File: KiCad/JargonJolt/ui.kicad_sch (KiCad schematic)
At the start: 18 parts, among them J4 Conn_01x06, J5 Conn_01x06, J6 Conn_01x08, J7 Conn_01x08, SW4 SW_Push, SW5 SW_Push, SW6 SW_Push, U4 74LVC3G17DP_125

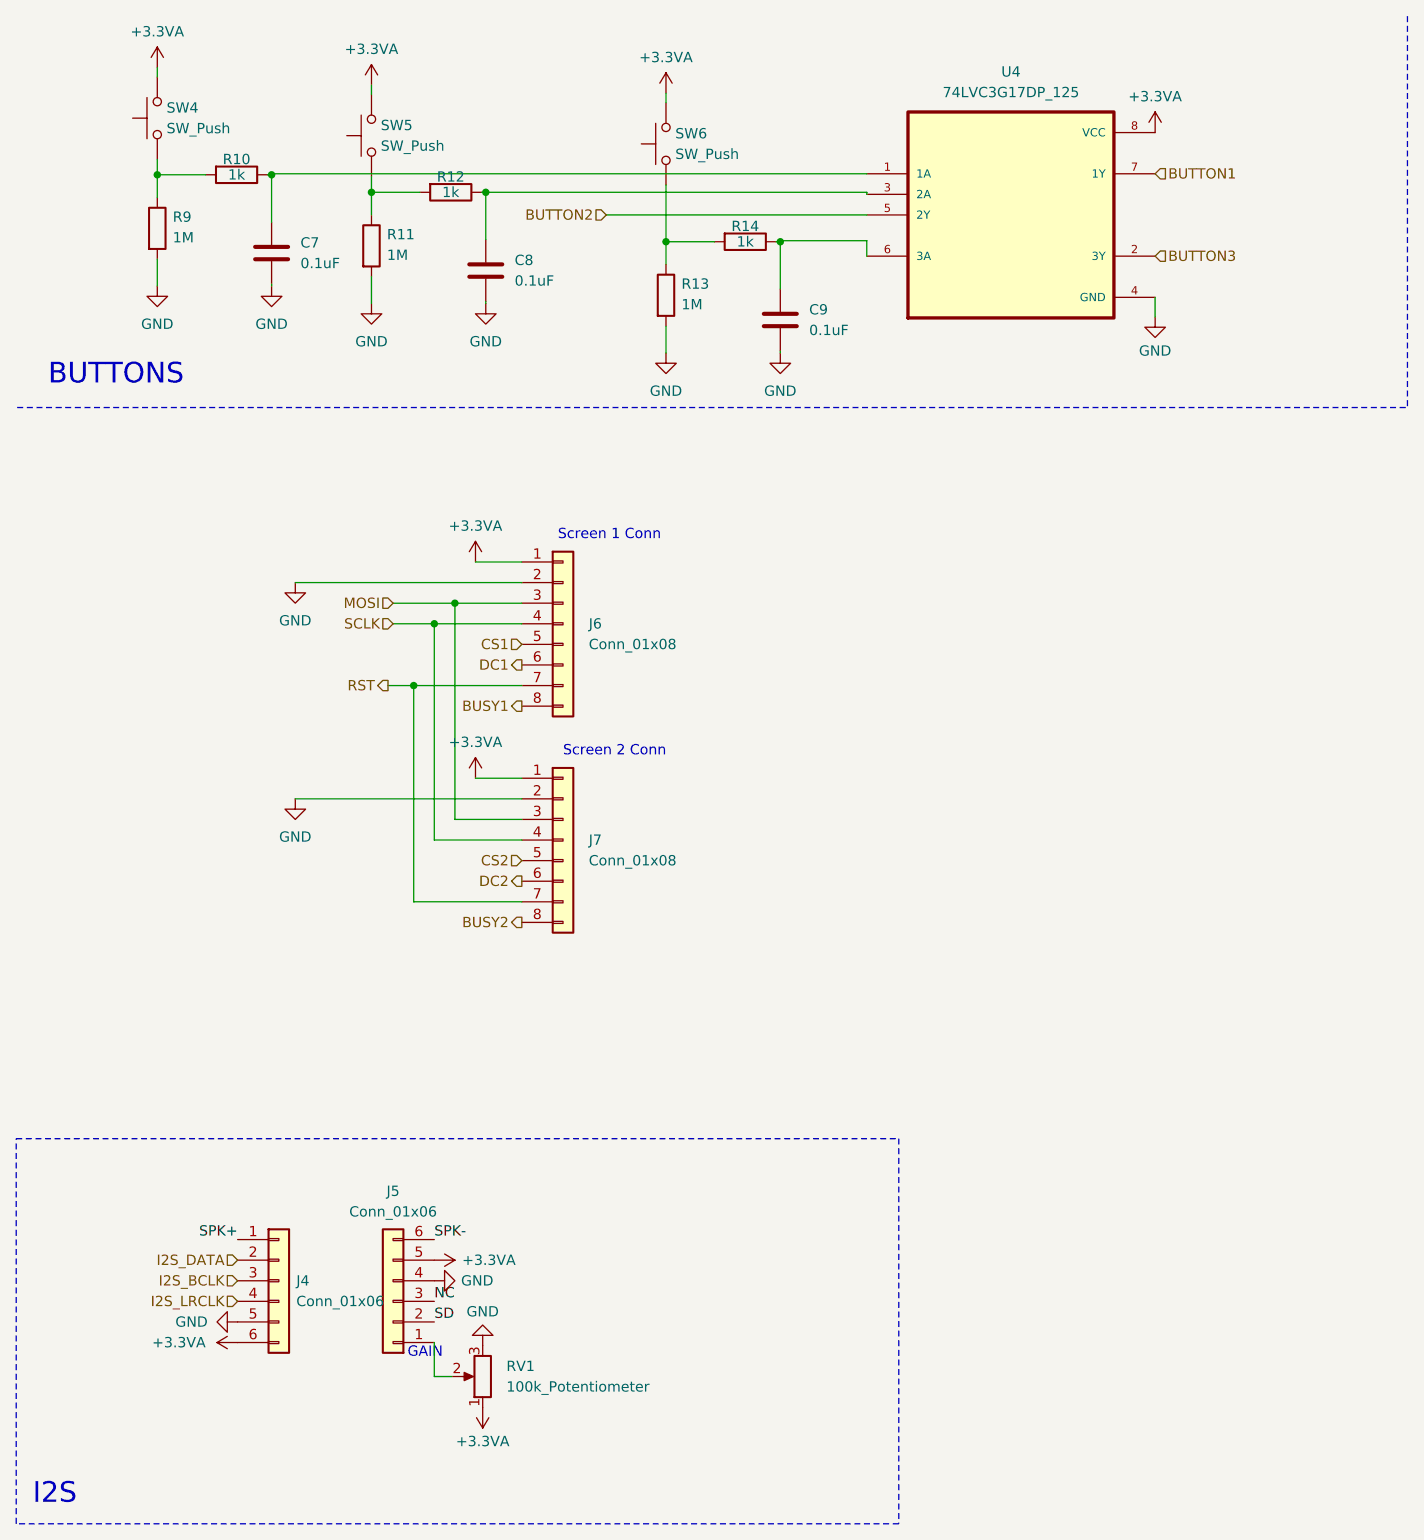
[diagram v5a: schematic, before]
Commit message: PCB first revision
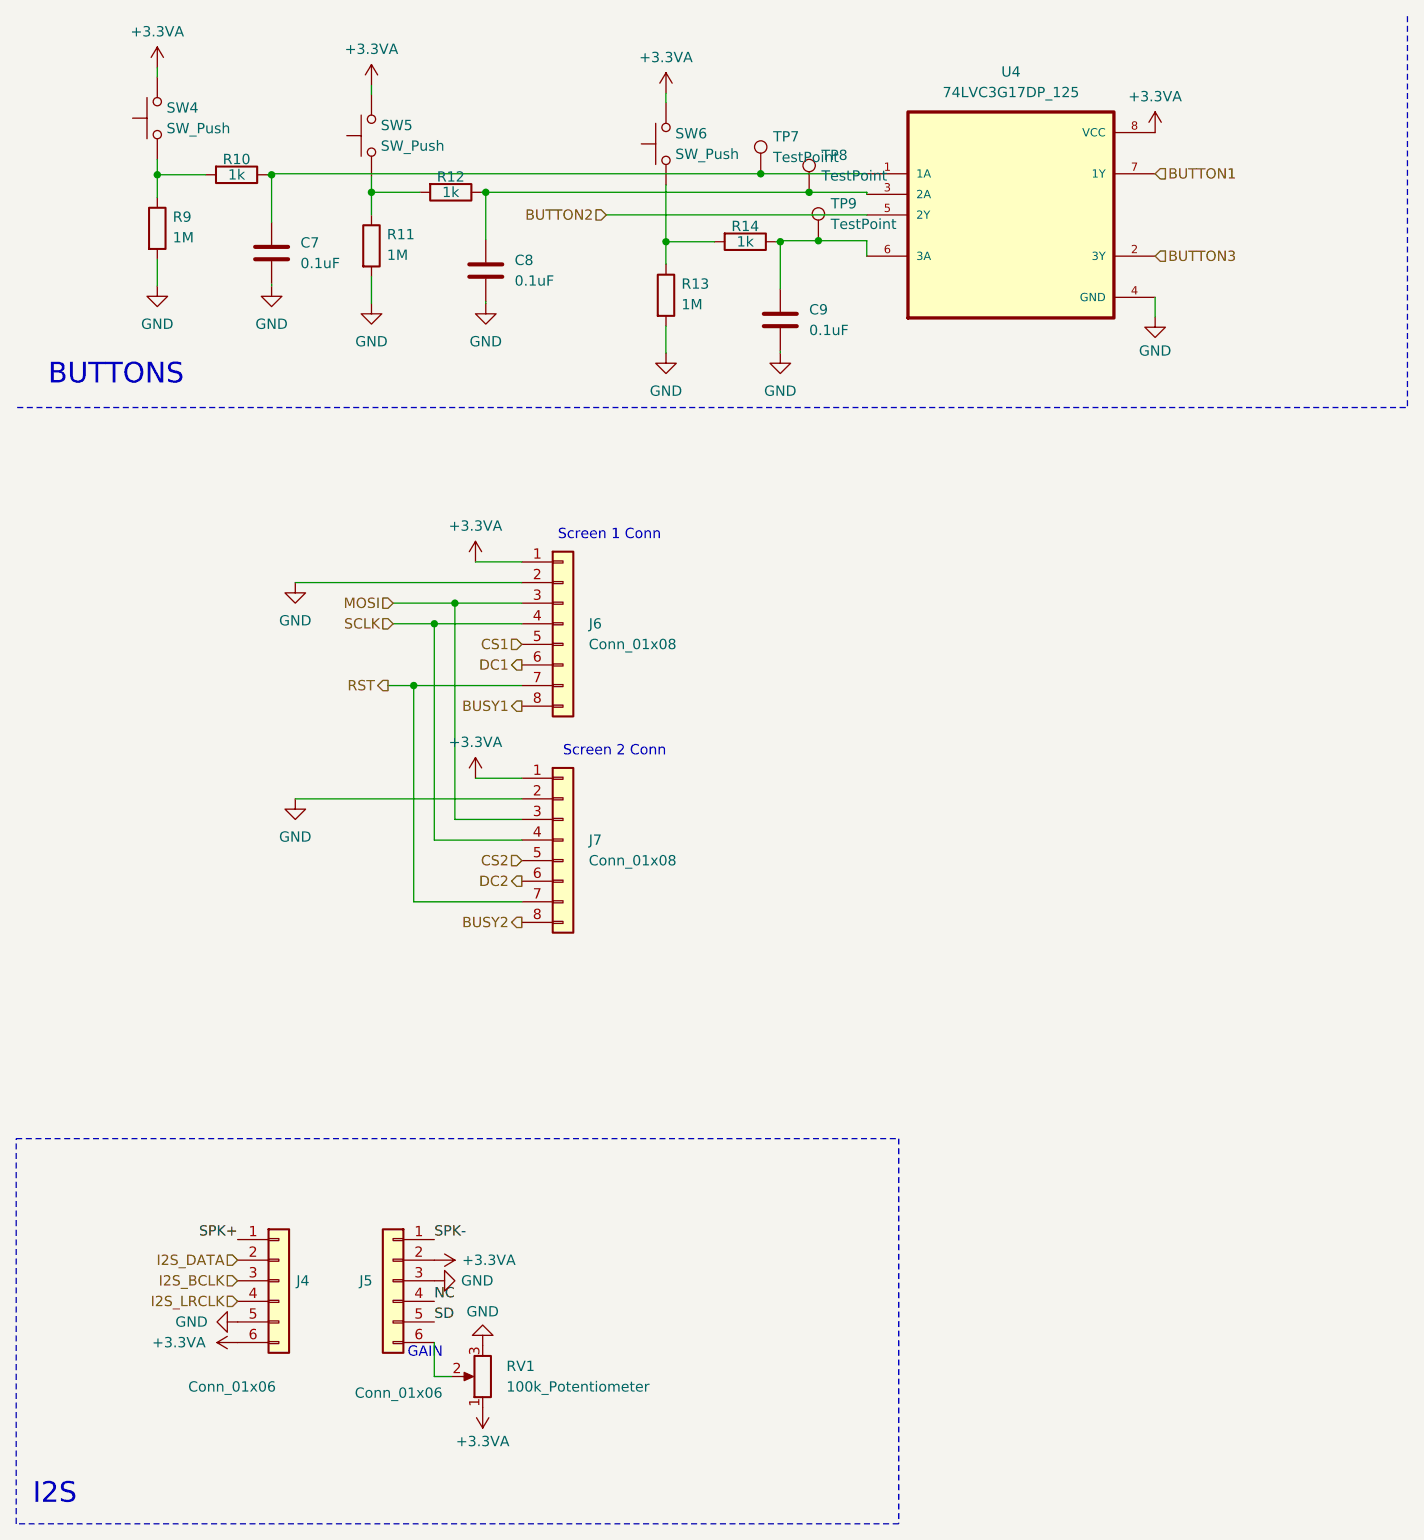
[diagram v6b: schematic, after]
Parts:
- added TP7, TP8, TP9: TestPoint, TestPoint:TestPoint_Pad_D1.5mm, symbol Connector:TestPoint
- SW4, SW5, SW6: footprint (none) -> Connector_Molex:Molex_KK-254_AE-6410-02A_1x02_P2.54mm_Vertical
- U4: footprint Espressif:SOP65P490X110-8N -> Package_SO:TSSOP-8_3x3mm_P0.65mm
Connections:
- net +3.3VA: now also J5.2 (Pin_2); no longer J5.5 (Pin_5)
- net GND: now also J5.3 (Pin_3); no longer J5.4 (Pin_4)
- net NC: now also J5.4 (Pin_4); no longer J5.3 (Pin_3)
- net SD: now also J5.5 (Pin_5); no longer J5.2 (Pin_2)
- net SPK-: now also J5.1 (Pin_1); no longer J5.6 (Pin_6)
- net at C9.1, R14.1, U4.6 (3A): now also TP9.1
- net at C7.1, R10.1, U4.1 (1A): now also TP7.1
- net at RV1.2: now also J5.6 (Pin_6); no longer J5.1 (Pin_1)
- net at C8.1, R12.1, U4.3 (2A): now also TP8.1
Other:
- moved on the sheet: J5
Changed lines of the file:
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@@
   (junction (at 43.434 31.623) (diameter 0) (color 0 0 0 0)
   )
+  (junction (at 103.759 31.496) (diameter 0) (color 0 0 0 0)
+  )
   (junction (at 66.04 84.455) (diameter 0) (color 0 0 0 0)
   )
@@
   (junction (at 106.172 39.878) (diameter 0) (color 0 0 0 0)
   )
+  (junction (at 109.728 33.782) (diameter 0) (color 0 0 0 0)
+  )
+  (junction (at 110.871 39.751) (diameter 0) (color 0 0 0 0)
+  )
   (junction (at 92.075 39.878) (diameter 0) (color 0 0 0 0)
   )
@@
     (stroke (width 0) (type default))
   )
-  (wire (pts (xy 69.85 33.782) (xy 116.84 33.782))
+  (wire (pts (xy 69.85 33.782) (xy 109.728 33.782))
     (stroke (width 0) (type default))
   )
   (wire (pts (xy 55.753 44.196) (xy 55.753 47.498))
-    (stroke (width 0) (type default))
-  )
-  (wire (pts (xy 63.5 175.641) (xy 63.5 179.832))
     (stroke (width 0) (type default))
   )
@@
     (stroke (width 0) (type dash))
   )
-  (wire (pts (xy 106.172 39.751) (xy 116.84 39.751))
+  (wire (pts (xy 106.172 39.751) (xy 110.871 39.751))
+    (stroke (width 0) (type default))
+  )
+  (wire (pts (xy 110.871 39.751) (xy 116.84 39.751))
     (stroke (width 0) (type default))
   )
@@
     (stroke (width 0) (type default))
   )
+  (wire (pts (xy 103.759 31.496) (xy 116.84 31.496))
+    (stroke (width 0) (type default))
+  )
   (wire (pts (xy 46.355 108.585) (xy 74.295 108.585))
     (stroke (width 0) (type default))
@@
     (stroke (width 0) (type default))
   )
-  (wire (pts (xy 43.434 31.496) (xy 116.84 31.496))
+  (wire (pts (xy 43.434 31.496) (xy 103.759 31.496))
     (stroke (width 0) (type default))
   )
@@
   )
   (wire (pts (xy 63.5 86.995) (xy 63.5 113.665))
+    (stroke (width 0) (type default))
+  )
+  (wire (pts (xy 109.728 33.782) (xy 116.84 33.782))
     (stroke (width 0) (type default))
   )
@@
   )
   (wire (pts (xy 55.753 33.782) (xy 61.722 33.782))
+    (stroke (width 0) (type default))
+  )
+  (wire (pts (xy 63.5 175.641) (xy 63.5 179.832))
     (stroke (width 0) (type default))
   )
@@
     )
   )
-  (symbol (lib_id "Connector_Generic:Conn_01x06") (at 58.42 170.561 180) (unit 1)
-    (in_bom yes) (on_board yes) (dnp no) (fields_autoplaced)
-    (property "Reference" "J5" (at 58.42 156.972 0)
-      (effects (font (size 1.27 1.27)))
-    )
-    (property "Value" "Conn_01x06" (at 58.42 159.512 0)
-      (effects (font (size 1.27 1.27)))
-    )
-    (property "Footprint" "Connector_PinHeader_2.54mm:PinHeader_1x06_P2.54mm_Vertical" (at 58.42 170.561 0)
-      (effects (font (size 1.27 1.27)) hide)
-    )
-    (property "Datasheet" "~" (at 58.42 170.561 0)
+  (symbol (lib_id "Connector_Generic:Conn_01x06") (at 58.42 168.021 0) (mirror y) (unit 1)
+    (in_bom yes) (on_board yes) (dnp no)
+    (property "Reference" "J5" (at 55.88 168.021 0)
+      (effects (font (size 1.27 1.27)) (justify left))
+    )
+    (property "Value" "Conn_01x06" (at 64.516 181.864 0)
+      (effects (font (size 1.27 1.27)) (justify left))
+    )
+    (property "Footprint" "Connector_PinHeader_2.54mm:PinHeader_1x06_P2.54mm_Vertical" (at 58.42 168.021 0)
+      (effects (font (size 1.27 1.27)) hide)
+    )
+    (property "Datasheet" "~" (at 58.42 168.021 0)
       (effects (font (size 1.27 1.27)) hide)
     )
@@
     )
   )
+  (symbol (lib_id "Connector:TestPoint") (at 103.759 31.496 0) (unit 1)
+    (in_bom yes) (on_board yes) (dnp no) (fields_autoplaced)
+    (property "Reference" "TP7" (at 105.283 26.924 0)
+      (effects (font (size 1.27 1.27)) (justify left))
+    )
+    (property "Value" "TestPoint" (at 105.283 29.464 0)
+      (effects (font (size 1.27 1.27)) (justify left))
+    )
+    (property "Footprint" "TestPoint:TestPoint_Pad_D1.5mm" (at 108.839 31.496 0)
+      (effects (font (size 1.27 1.27)) hide)
+    )
+    (property "Datasheet" "~" (at 108.839 31.496 0)
+      (effects (font (size 1.27 1.27)) hide)
+    )
+    (pin "1")
+    (instances
+      (project "JargonJolt"
+        (path "/39fa52d1-bab8-41e3-aba2-e2f783adaf1f/80b8e0d4-b7c3-4d2a-a6d1-a18c3cb1cfc9"
+          (reference "TP7") (unit 1)
+        )
+      )
+    )
+  )
   (symbol (lib_id "Device:R") (at 55.753 40.386 0) (unit 1)
     (in_bom yes) (on_board yes) (dnp no)
@@
       (effects (font (size 1.27 1.27)))
     )
-    (property "Footprint" "Espressif:SOP65P490X110-8N" (at 134.62 36.576 0)
+    (property "Footprint" "Package_SO:TSSOP-8_3x3mm_P0.65mm" (at 134.62 36.576 0)
       (effects (font (size 1.27 1.27)) (justify bottom) hide)
     )
-    (property "Datasheet" "" (at 134.62 36.576 0)
+    (property "Datasheet" "https://www.mouser.com/datasheet/2/916/74LVC3G17-1541796.pdf" (at 134.62 36.576 0)
       (effects (font (size 1.27 1.27)) hide)
     )
@@
       (effects (font (size 1.27 1.27)) (justify right))
     )
-    (property "Footprint" "" (at 50.673 26.797 0)
+    (property "Footprint" "Connector_Molex:Molex_KK-254_AE-6410-02A_1x02_P2.54mm_Vertical" (at 50.673 26.797 0)
       (effects (font (size 1.27 1.27)) hide)
     )
@@
       (effects (font (size 1.27 1.27)) (justify left))
     )
-    (property "Value" "Conn_01x06" (at 46.482 170.561 0)
+    (property "Value" "Conn_01x06" (at 33.147 181.102 0)
       (effects (font (size 1.27 1.27)) (justify left))
     )
@@
       (effects (font (size 1.27 1.27)) (justify right))
     )
-    (property "Footprint" "" (at 86.995 27.813 0)
+    (property "Footprint" "Connector_Molex:Molex_KK-254_AE-6410-02A_1x02_P2.54mm_Vertical" (at 86.995 27.813 0)
       (effects (font (size 1.27 1.27)) hide)
     )
@@
     )
   )
+  (symbol (lib_id "Connector:TestPoint") (at 109.728 33.782 0) (unit 1)
+    (in_bom yes) (on_board yes) (dnp no) (fields_autoplaced)
+    (property "Reference" "TP8" (at 111.252 29.21 0)
+      (effects (font (size 1.27 1.27)) (justify left))
+    )
+    (property "Value" "TestPoint" (at 111.252 31.75 0)
+      (effects (font (size 1.27 1.27)) (justify left))
+    )
+    (property "Footprint" "TestPoint:TestPoint_Pad_D1.5mm" (at 114.808 33.782 0)
+      (effects (font (size 1.27 1.27)) hide)
+    )
+    (property "Datasheet" "~" (at 114.808 33.782 0)
+      (effects (font (size 1.27 1.27)) hide)
+    )
+    (pin "1")
+    (instances
+      (project "JargonJolt"
+        (path "/39fa52d1-bab8-41e3-aba2-e2f783adaf1f/80b8e0d4-b7c3-4d2a-a6d1-a18c3cb1cfc9"
+          (reference "TP8") (unit 1)
+        )
+      )
+    )
+  )
   (symbol (lib_id "Switch:SW_Push") (at 29.337 24.638 90) (unit 1)
     (in_bom yes) (on_board yes) (dnp no) (fields_autoplaced)
@@
       (effects (font (size 1.27 1.27)) (justify right))
     )
-    (property "Footprint" "" (at 24.257 24.638 0)
+    (property "Footprint" "Connector_Molex:Molex_KK-254_AE-6410-02A_1x02_P2.54mm_Vertical" (at 24.257 24.638 0)
       (effects (font (size 1.27 1.27)) hide)
     )
@@
         )
       )
+    )
+  )
+  (symbol (lib_id "Connector:TestPoint") (at 110.871 39.751 0) (unit 1)
+    (in_bom yes) (on_board yes) (dnp no) (fields_autoplaced)
+    (property "Reference" "TP9" (at 112.395 35.179 0)
+      (effects (font (size 1.27 1.27)) (justify left))
+    )
+    (property "Value" "TestPoint" (at 112.395 37.719 0)
+      (effects (font (size 1.27 1.27)) (justify left))
+    )
+    (property "Footprint" "TestPoint:TestPoint_Pad_D1.5mm" (at 115.951 39.751 0)
+      (effects (font (size 1.27 1.27)) hide)
+    )
+    (property "Datasheet" "~" (at 115.951 39.751 0)
+      (effects (font (size 1.27 1.27)) hide)
+    )
+    (pin "1")
+    (instances
+      (project "JargonJolt"
+        (path "/39fa52d1-bab8-41e3-aba2-e2f783adaf1f/80b8e0d4-b7c3-4d2a-a6d1-a18c3cb1cfc9"
+          (reference "TP9") (unit 1)
+        )
+      )
